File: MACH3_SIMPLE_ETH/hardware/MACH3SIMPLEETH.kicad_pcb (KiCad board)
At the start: 4 copper layers, 210 x 155 mm, 337 parts, among them J101 SENSORS / 24V IN, J201 USB-C, J202 SWD, J203 microSD, J301 HR911105A, J401 X axis, J402 Y axis, J403 Z axis, J404 A axis, J405 B axis, J406 C axis, J407 U axis, J408 V axis, J409 ENABLE, J501 LIMITS X Y Z A B C U V, J502 EST HLD RUN PRB, J503 THC AOK UP DN, J601 EXPANSION, J611 Relay A, J612 Relay B, J613 Relay C, J614 Relay D, J615 Relay E, J616 Relay F, J701 VFD, J801 RS485 A B GND, J802 HW ICSP, J803 MPG PENDANT, K601 JQC-3FF-024-1Z, K602 JQC-3FF-024-1Z, K603 JQC-3FF-024-1Z, K604 JQC-3FF-024-1Z, K605 JQC-3FF-024-1Z, K606 JQC-3FF-024-1Z, Q601 AO3400A, Q602 AO3400A, Q603 AO3400A, Q604 AO3400A, Q605 AO3400A, Q606 AO3400A, SW201 RESET, SW202 BOOTSEL, U101 LM2596S-5, U102 AP7361C-33E, U201 RP2350B, U202 W25Q128JVS, U203 USBLC6-2SC6, U301 W5500, U401 74ACT245, U402 74ACT245, U403 74ACT245, U501 PC847, U502 PC847, U503 PC847, U504 PC847, U601 MCP23017-E/SO, U701 74HCT14, U702 PC847, U703 B2412S-1WR3, U704 78L05, U705 LM358, U801 MAX3485ESA, U802 ATmega328P-AU, Y201 12MHz ABM8-272-T3, Y301 25MHz 18pF, Y801 8MHz

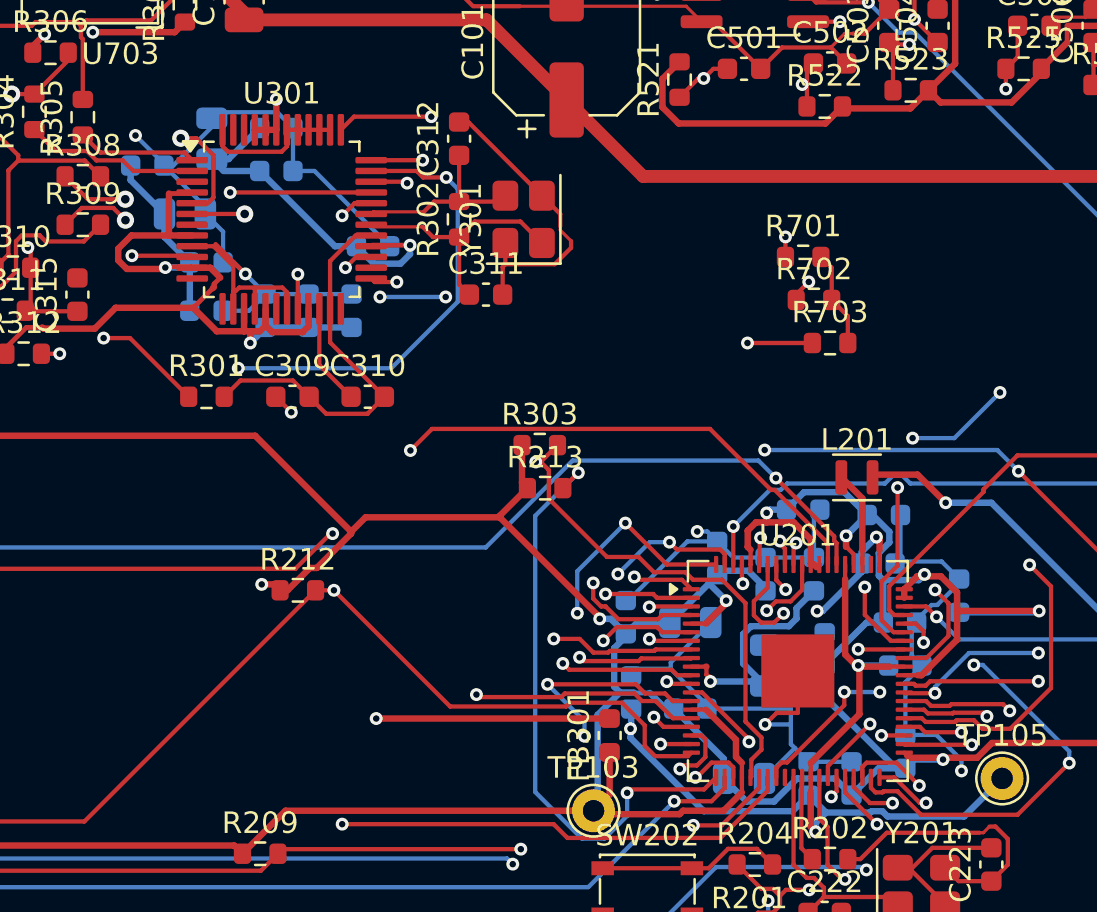
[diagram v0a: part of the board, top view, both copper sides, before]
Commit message: MACH3-SIMPLE-ETH: repair router starts at the pin; cleanup of stray vias
Two GND repairs had started from the already-connected end and dropped a
via next to copper that was on the plane already, leaving the pin open.
Repairs now start at the U/J pin; holes get 0.1 mm more margin; duplicate
and dangling vias are removed; the VBUS repair too close to J201's hole is
taken up to be routed again.

Co-Authored-By: Claude Opus 5.5 <noreply@anthropic.com>
Claude-Session: https://claude.ai/code/session_01MByiLT2xCcbGPkgCYQy33q
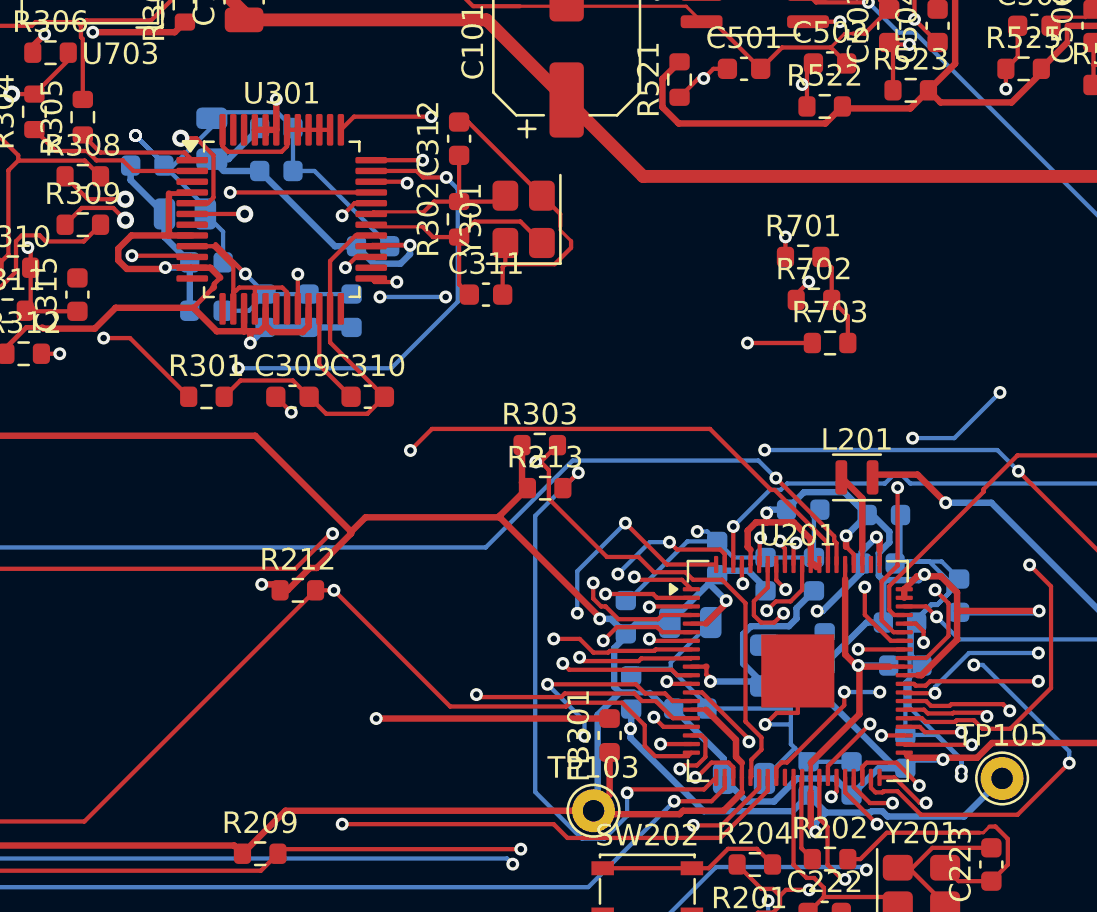
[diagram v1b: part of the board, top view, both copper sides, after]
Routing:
- net GND: track 708.3 -> 723.2 mm, vias 5 -> 7
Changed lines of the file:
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@@
+	)
+	(via
+		(at 69.6 90.9)
+		(size 0.6)
+		(drill 0.3)
+		(layers "F.Cu" "B.Cu")
+		(net "GND")
 	)
 	(via
@@
 	)
 	(via
+		(at 31.2 61.1)
+		(size 0.6)
+		(drill 0.3)
+		(layers "F.Cu" "B.Cu")
+		(net "GND")
+	)
+	(via
 		(at 60.4806 88.487)
 		(size 0.6)
@@
 	)
 	(segment
+		(start 67.2 87.7)
+		(end 69.6 90.1)
+		(width 0.2)
+		(layer "B.Cu")
+		(net "GND")
+	)
+	(segment
 		(start 57.775 87.586)
 		(end 56.0901 85.9011)
@@
 	)
 	(segment
+		(start 68.2 82.9)
+		(end 67.2 83.9)
+		(width 0.2)
+		(layer "B.Cu")
+		(net "GND")
+	)
+	(segment
 		(start 61.6763 87.75)
 		(end 57.775 87.75)
@@
 	)
 	(segment
+		(start 69 81.8)
+		(end 69 82.4)
+		(width 0.2)
+		(layer "B.Cu")
+		(net "GND")
+	)
+	(segment
 		(start 67 86.525)
 		(end 67 88.975)
@@
 	)
 	(segment
+		(start 69 82.4)
+		(end 68.5 82.9)
+		(width 0.2)
+		(layer "B.Cu")
+		(net "GND")
+	)
+	(segment
 		(start 38.525 60.75)
 		(end 38.525 62.75)
@@
 	)
 	(segment
+		(start 68.5 82.9)
+		(end 68.2 82.9)
+		(width 0.2)
+		(layer "B.Cu")
+		(net "GND")
+	)
+	(segment
 		(start 37.7935 60.0185)
 		(end 38.525 60.75)
@@
 	)
 	(segment
+		(start 32.2 62.1)
+		(end 31.2 61.1)
+		(width 0.2)
+		(layer "B.Cu")
+		(net "GND")
+	)
+	(segment
 		(start 56.0901 85.9011)
 		(end 54.5739 85.9011)
@@
 	)
 	(segment
+		(start 66.9 80.9)
+		(end 68.1 80.9)
+		(width 0.2)
+		(layer "B.Cu")
+		(net "GND")
+	)
+	(segment
 		(start 41.25 68.475)
 		(end 39.25 68.475)
@@
 	)
 	(segment
+		(start 69.6 90.1)
+		(end 69.6 90.9)
+		(width 0.2)
+		(layer "B.Cu")
+		(net "GND")
+	)
+	(segment
 		(start 61.8625 89.5875)
 		(end 61.6763 89.4013)
@@
 	)
 	(segment
+		(start 67.2 83.9)
+		(end 67.2 87.7)
+		(width 0.2)
+		(layer "B.Cu")
+		(net "GND")
+	)
+	(segment
 		(start 69.5 81.725)
 		(end 68.6856 80.9106)
@@
 		(width 0.2)
 		(layer "B.Cu")
+		(net "GND")
+	)
+	(segment
+		(start 68.1 80.9)
+		(end 69 81.8)
+		(width 0.2)
+		(layer "B.Cu")
